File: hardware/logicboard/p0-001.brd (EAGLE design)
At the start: 91 x 57 mm, 24 parts, among them IC1 74ALS05N, IC2 LTC485N, IC3 LTC485N, J0 DC5V, J1 DIN5, J2 DIN5, J3 DIN5, X1 NELTRON-7810-XPXC, X2 NELTRON-7810-XPXC

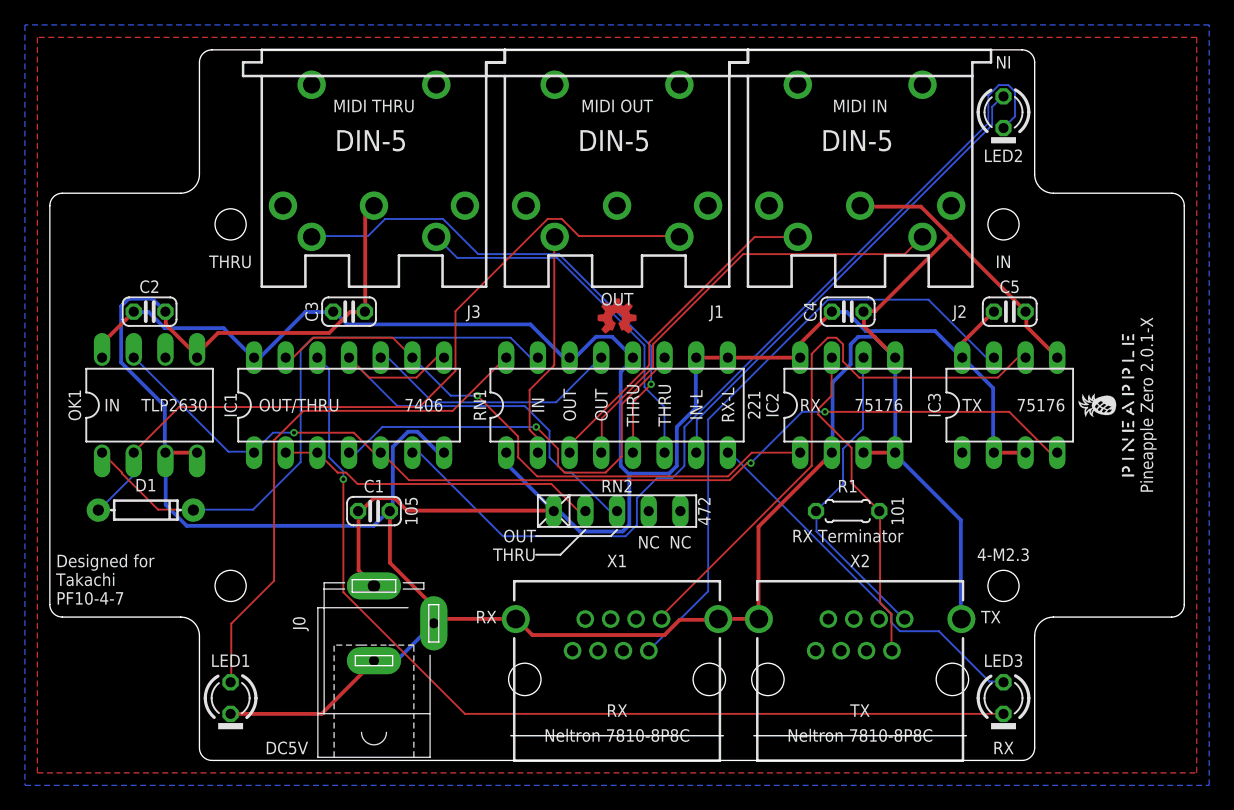
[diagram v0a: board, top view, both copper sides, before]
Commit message: Fixed pull-up.
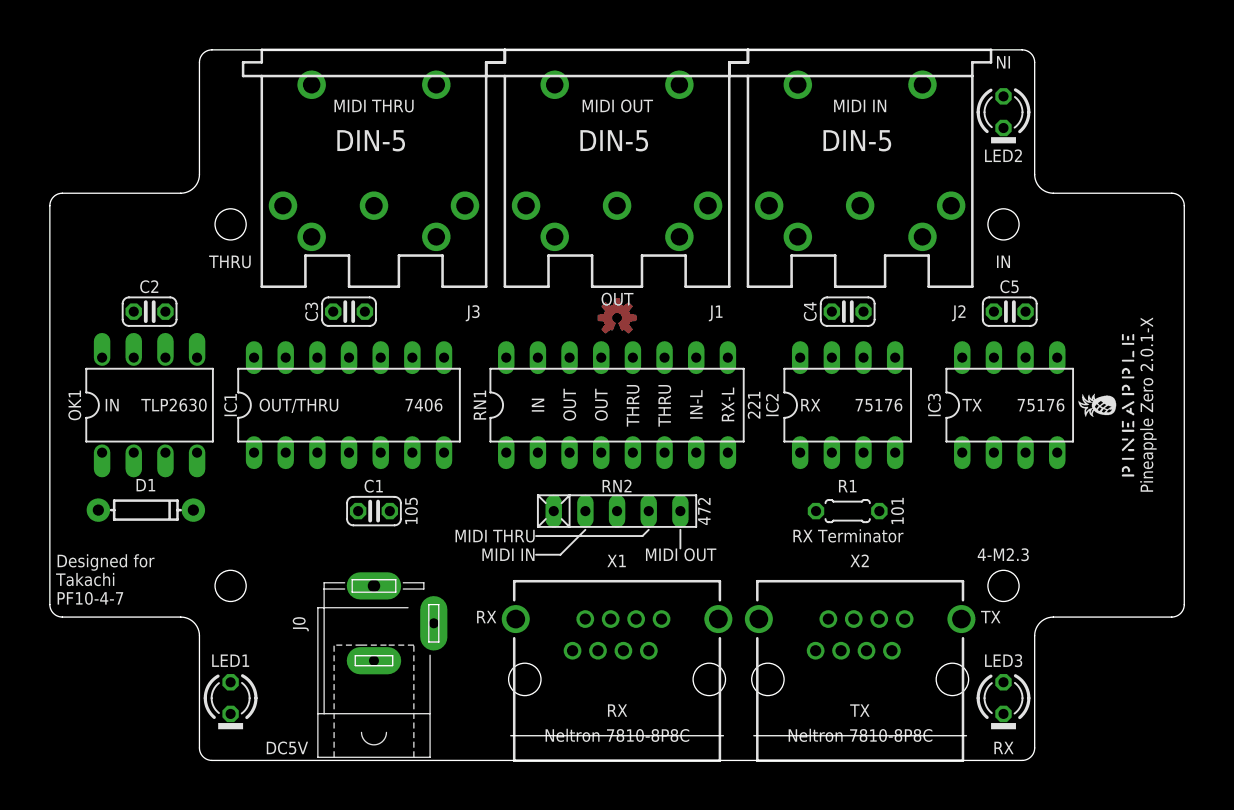
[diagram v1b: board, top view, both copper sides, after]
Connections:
- net NMIDIOUT: now also RN2.5; no longer RN2.3
- net NMIDITHRU: now also RN2.4; no longer RN2.2
- net TX: now also RN2.2
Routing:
- net GND: track 231.0 -> 0.00 mm
- net VCC: track 155.7 -> 0.00 mm
- net TX: track 83.2 -> 0.00 mm, vias 3 -> 0
- net RXLED: track 76.7 -> 0.00 mm, vias 1 -> 0
- net MIDIINLED: track 74.0 -> 0.00 mm
- net MIRTN: track 60.8 -> 0.00 mm
- net TX-: track 49.4 -> 0.00 mm
- net MIDIIN: track 48.6 -> 0.00 mm
- net RX: track 48.3 -> 0.00 mm, vias 1 -> 0
- net TX+: track 46.7 -> 0.00 mm
- net PWRLED: track 42.2 -> 0.00 mm
- net MTSND: track 41.2 -> 0.00 mm, vias 1 -> 0
- net MIDIINLEDA: track 38.8 -> 0.00 mm
- net NMIDIOUT: track 36.8 -> 0.00 mm
- net MORTN: track 35.6 -> 0.00 mm
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- removed copper zone on layer 1, net GND
- removed copper zone on layer 16, net GND
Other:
- board text removed: "NC"

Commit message: Swapped MIDI IN and THRU, TX and RX.
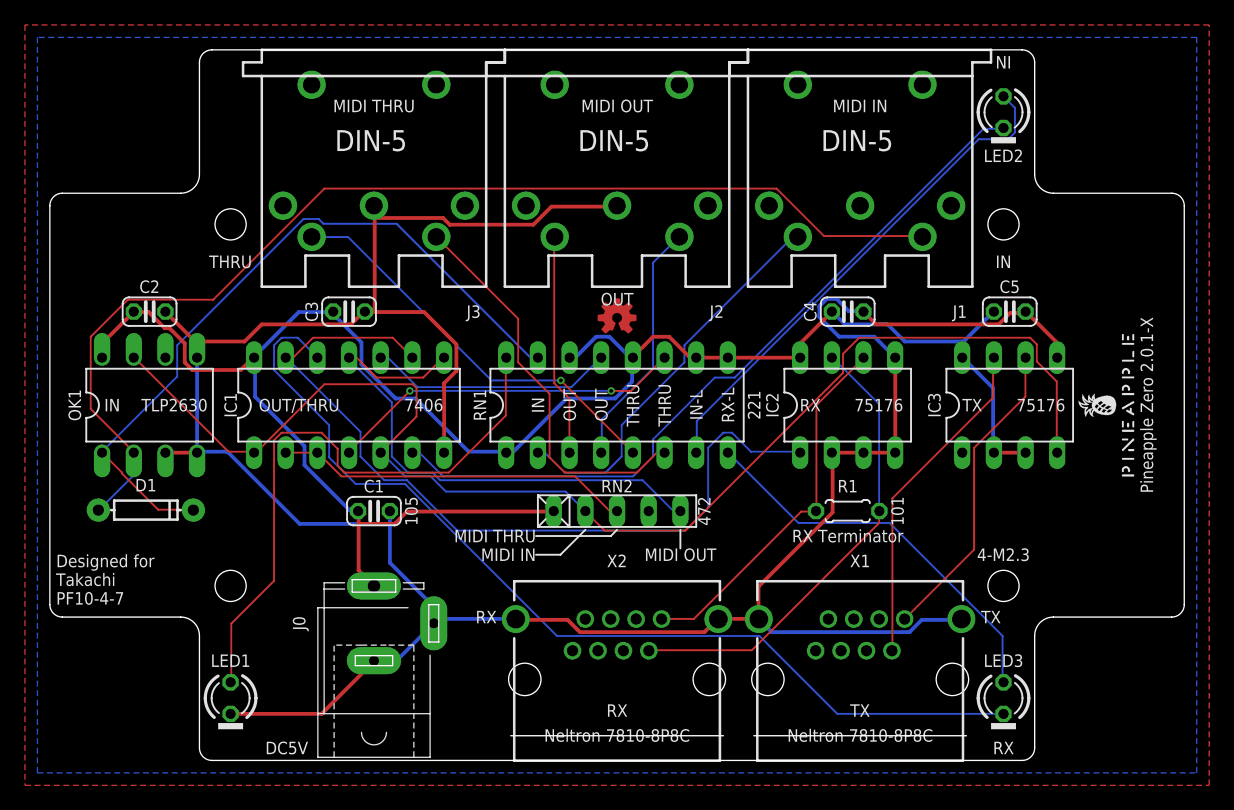
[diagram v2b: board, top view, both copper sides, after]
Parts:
- moved J1 19.5 mm to (65.0, 57.0)
- moved J2 19.5 mm to (45.5, 57.0)
- moved X1 19.5 mm to (65.0, 6.50)
- moved X2 19.5 mm to (45.5, 6.50)
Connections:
- net NMIDITHRU: now also RN2.3; no longer RN2.4
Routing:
- net GND: track 0.00 -> 229.7 mm
- net VCC: track 0.00 -> 153.1 mm
- net TX: track 0.00 -> 106.7 mm
- net MIRTN: track 0.00 -> 89.8 mm
- net RXLED: track 0.00 -> 77.8 mm
- net RX: track 0.00 -> 66.4 mm
- net MIDIINLED: track 0.00 -> 60.6 mm
- net MIDIIN: track 0.00 -> 58.1 mm
- net PWRLED: track 0.00 -> 48.4 mm
- net NMIDIOUT: track 0.00 -> 43.3 mm
- net MIDIINLEDA: track 0.00 -> 40.9 mm
- net RX-: track 0.00 -> 37.6 mm
- net MTSND: track 0.00 -> 32.9 mm, vias 0 -> 1
- net RXLEDA: track 0.00 -> 31.9 mm
- net MTRTN: track 0.00 -> 31.9 mm
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- added copper zone on layer 1, net GND
- added copper zone on layer 16, net GND

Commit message: Changed wiring of MIDI IN LED.
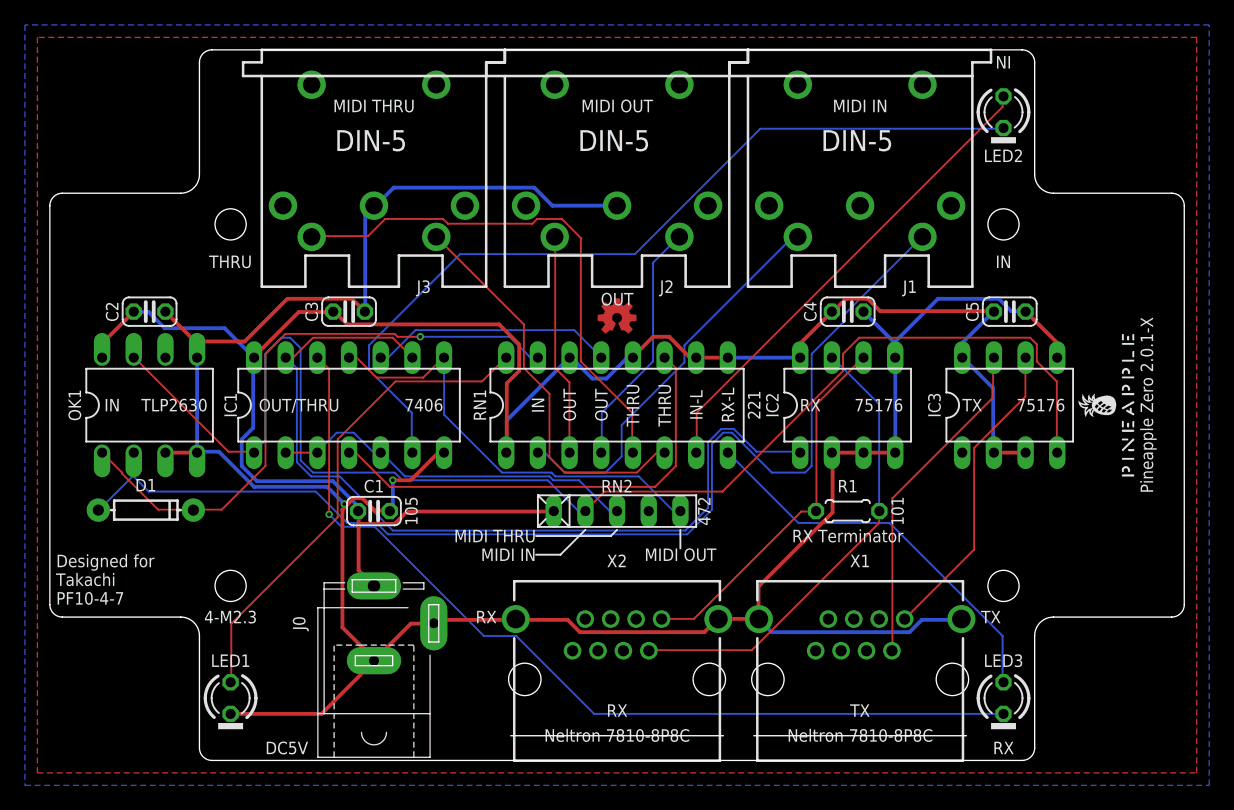
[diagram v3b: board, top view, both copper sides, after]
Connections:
- net NMIDITHRU: now also IC1.5
- net TX: no longer IC1.5
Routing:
- net GND: track 229.7 -> 215.3 mm, vias 0 -> 2
- net MIDIIN: track 58.1 -> 48.8 mm, vias 0 -> 1
- net MTSND: track 32.9 -> 42.1 mm, vias 1 -> 0
- net PWRLED: track 48.4 -> 39.3 mm
- net MIDITHRU: track 28.5 -> 37.1 mm, vias 2 -> 0
- net NMIDIOUT: track 43.3 -> 35.7 mm
- net MIDIINLED: track 60.6 -> 68.2 mm
- net MIRTN: track 89.8 -> 94.1 mm
- net RXLED: track 77.8 -> 73.7 mm, vias 0 -> 1
- net VCC: track 153.1 -> 157.3 mm
- net TX: track 106.7 -> 110.7 mm
- net RX: track 66.4 -> 70.2 mm
- net MIDIINLEDA: track 40.9 -> 38.8 mm
- net NMIDITHRU: track 28.5 -> 29.9 mm

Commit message: Changed Rs for LEDs.
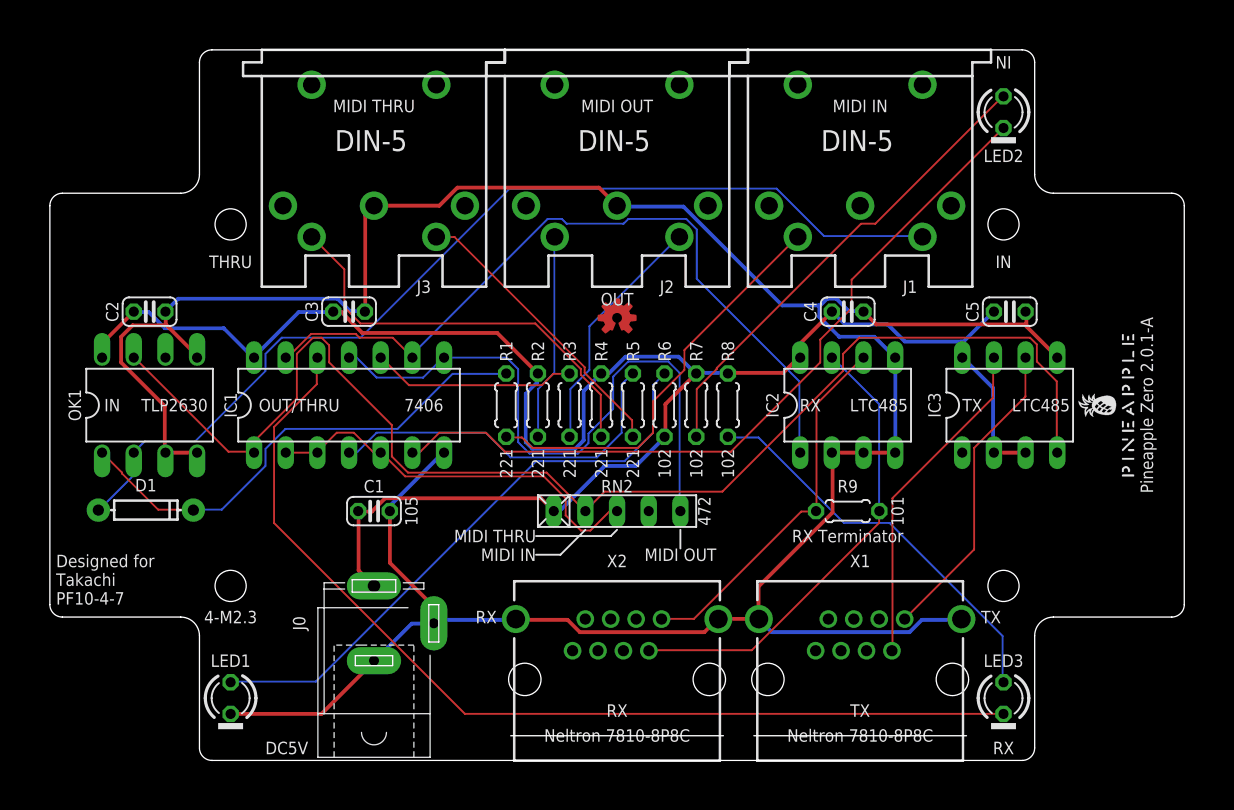
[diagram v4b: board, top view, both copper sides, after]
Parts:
- removed RN1: 220, resistor-dil:DIL16
- added R2, R3, R4, R5: 220, rcl:0204/5
- added R6, R7, R8: 1k, rcl:0204/5
- added R9: 100, rcl:0204/5
- R1: value 100 -> 220
- moved R1 28.7 mm to (36.6, 28.5), turned to 90 degrees
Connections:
- net MIDIIN: now also R1.2; no longer RN1.15
- net MIDIINLEDA: now also R7.1; no longer RN1.7
- net MIDIOUT: now also R3.2; no longer RN1.13
- net MIDITHRU: now also R5.2; no longer RN1.11
- net MISND: now also R1.1; no longer RN1.2
- net MORTN: now also R3.1; no longer RN1.4
- net MOSND: now also R2.1; no longer RN1.3
- net MTRTN: now also R5.1; no longer RN1.6
- net MTSND: now also R4.1; no longer RN1.5
- net PWRLED: now also R6.2; no longer RN1.16
- net RX+: now also R9.1; no longer R1.1
- net RX-: now also R9.2; no longer R1.2
- net RXLEDA: now also R8.1; no longer RN1.8
- net VCC: now also R2.2, R4.2, R6.1, R7.2, R8.2; no longer RN1.1, RN1.10, RN1.12, RN1.14, RN1.9
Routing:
- net NMIDIOUT: track 35.7 -> 51.0 mm
- net MIRTN: track 94.1 -> 80.3 mm
- net GND: track 215.3 -> 227.8 mm, vias 2 -> 0
- net MIDIIN: track 48.8 -> 39.7 mm, vias 1 -> 0
- net RX: track 70.2 -> 61.3 mm
- net MTRTN: track 31.9 -> 23.4 mm
- net MTSND: track 42.1 -> 33.9 mm
- net PWRLED: track 39.3 -> 47.3 mm
- net MIDITHRU: track 37.1 -> 29.4 mm
- net VCC: track 157.3 -> 151.0 mm
- net MIDIINLED: track 68.2 -> 61.9 mm
- net RXLED: track 73.7 -> 79.6 mm, vias 1 -> 0
- net TX: track 110.7 -> 106.3 mm
- net MIDIOUT: track 19.5 -> 16.5 mm
- net NMIDITHRU: track 29.9 -> 32.0 mm
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- removed copper zone on layer 1, net GND
- removed copper zone on layer 16, net GND
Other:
- board text added: "102"
- board text added: "LTC485"
- board text added: "Pineapple Zero 2.0.1-A"
- board text removed: "75176"
- board text removed: "IN-L"
- board text removed: "Pineapple Zero 2.0.1-X"
- board text removed: "RX-L"

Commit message: Added MIDI signal checker.
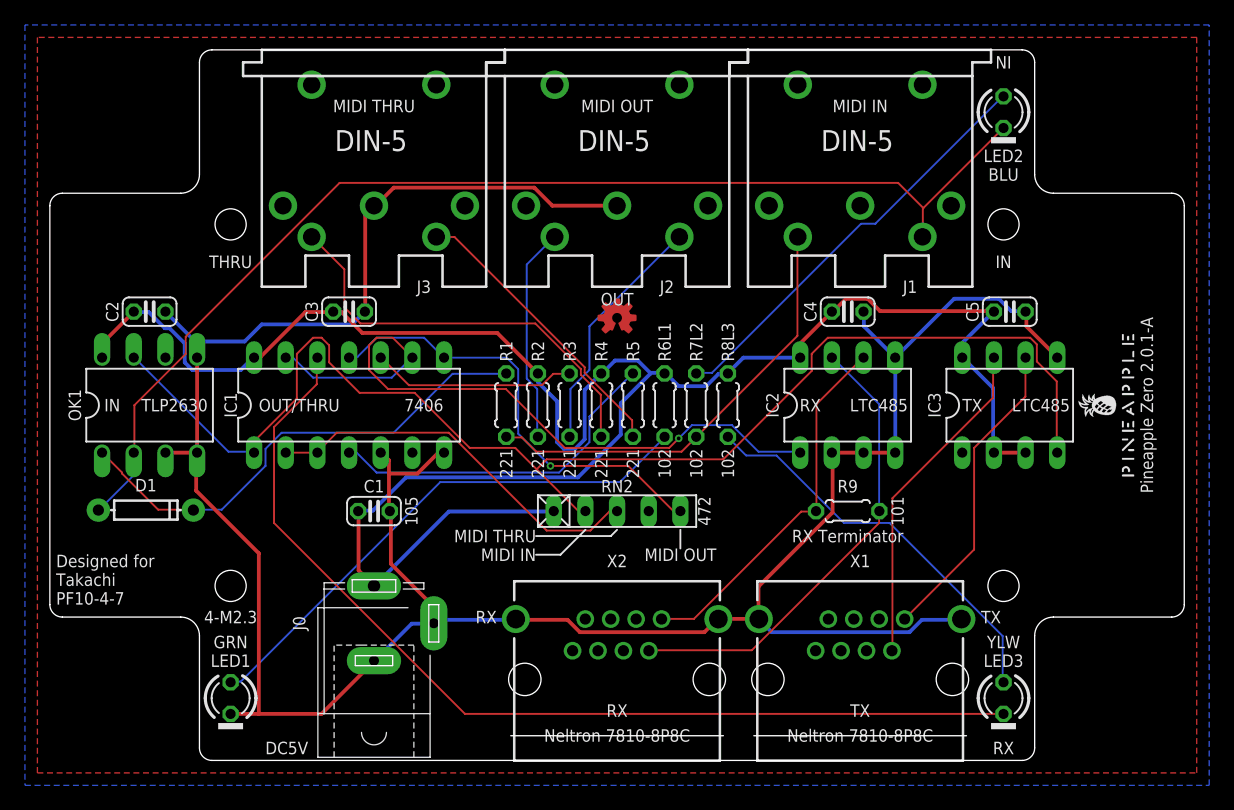
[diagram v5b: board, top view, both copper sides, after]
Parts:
- LED1: value GREEN -> BLUE
- LED2: value RED -> YELLOW
- renumbered R6 to R6L1, R7 to R7L2, R8 to R8L3
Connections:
- net RXLED renamed N$3
- net RXLEDA renamed N$2
- removed net MIDIINLED: IC1.6, LED2.K
- removed net MIDIINLEDA: LED2.A, R7L2.1
- removed net PWRLED: LED1.A, R6L1.2
- new net N$1: LED2.A, R7L2.2
- new net N$4: LED1.A, R6L1.1
- net GND: now also IC1.5
- net MIRTN: now also LED2.K
- net MISND: now also R7L2.1
- net NMIDITHRU: no longer IC1.5
- net VCC: now also R6L1.2; no longer R6L1.1, R7L2.2
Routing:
- net MIDIINLED: track 61.9 -> 0.00 mm
- net PWRLED: track 47.3 -> 0.00 mm
- net N$4: track 0.00 -> 43.0 mm
- net MIDIINLEDA: track 38.2 -> 0.00 mm
- net N$1: track 0.00 -> 33.9 mm
- net NMIDIOUT: track 51.0 -> 36.1 mm, vias 0 -> 1
- net VCC: track 151.0 -> 164.5 mm
- net MIRTN: track 80.3 -> 93.4 mm
- net GND: track 227.8 -> 218.2 mm
- net RX: track 61.3 -> 56.7 mm, vias 0 -> 1
- net MISND: track 33.2 -> 35.7 mm
- net MIDITHRU: track 29.4 -> 27.9 mm
- net TX: track 106.3 -> 107.3 mm
- net NMIDITHRU: track 32.0 -> 31.2 mm
- net MOSND: track 16.6 -> 17.4 mm
- added copper zone on layer 1, net GND
- added copper zone on layer 16, net GND
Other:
- board text added: "BLU"
- board text added: "GRN"
- board text added: "YLW"

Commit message: Changed led connection.
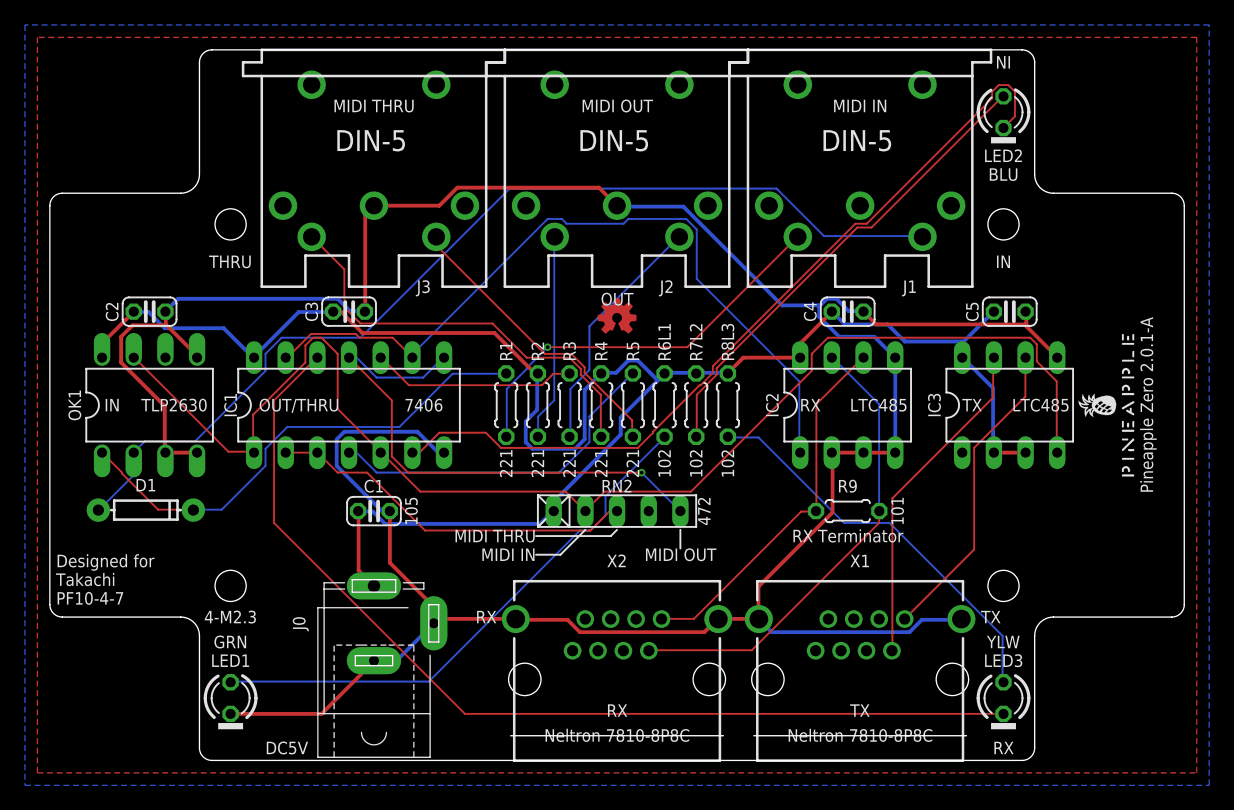
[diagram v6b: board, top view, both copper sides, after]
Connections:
- new net N$5: LED2.A, R7L2.1
- net GND: no longer IC1.5
- net MIRTN: no longer LED2.K
- net MISND: no longer R7L2.1
- net N$1: now also IC1.6, LED2.K; no longer LED2.A, R7L2.2
- net TX: now also IC1.5
- net VCC: now also R7L2.2
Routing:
- net N$5: track 0.00 -> 38.2 mm
- net N$1: track 33.9 -> 65.8 mm
- net GND: track 218.2 -> 238.8 mm
- net VCC: track 164.5 -> 147.6 mm
- net MIRTN: track 93.4 -> 80.3 mm
- net NMIDIOUT: track 36.1 -> 43.3 mm
- net RX: track 56.7 -> 61.3 mm, vias 1 -> 0
- net MISND: track 35.7 -> 32.3 mm, vias 0 -> 1
- net NMIDITHRU: track 31.2 -> 29.8 mm
- net N$4: track 43.0 -> 43.9 mm
- net MOSND: track 17.4 -> 16.6 mm
- net TX: track 107.3 -> 106.6 mm
